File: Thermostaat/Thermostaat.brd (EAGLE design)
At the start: 79.7 x 60.2 mm, 30 parts, among them IC2 MEGA8-P

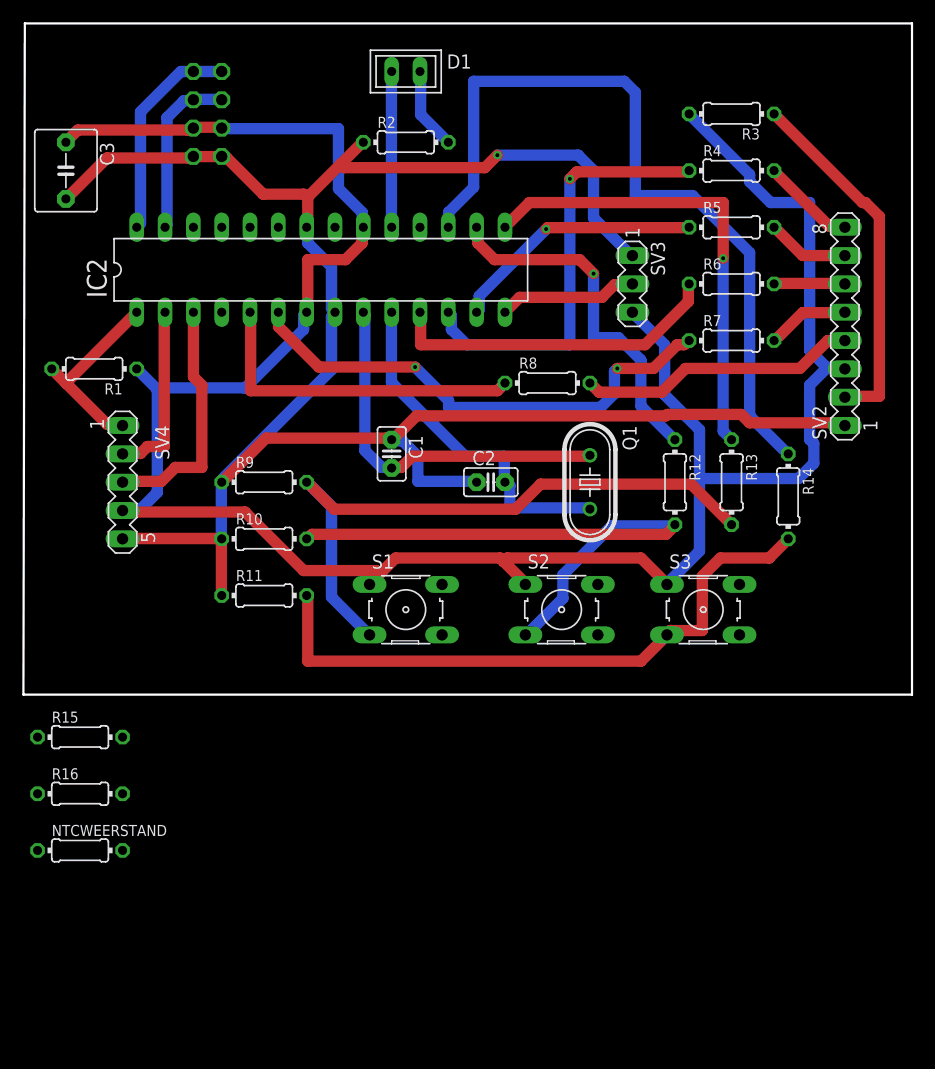
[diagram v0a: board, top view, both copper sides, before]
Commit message: transistor toegevoegd voor relais
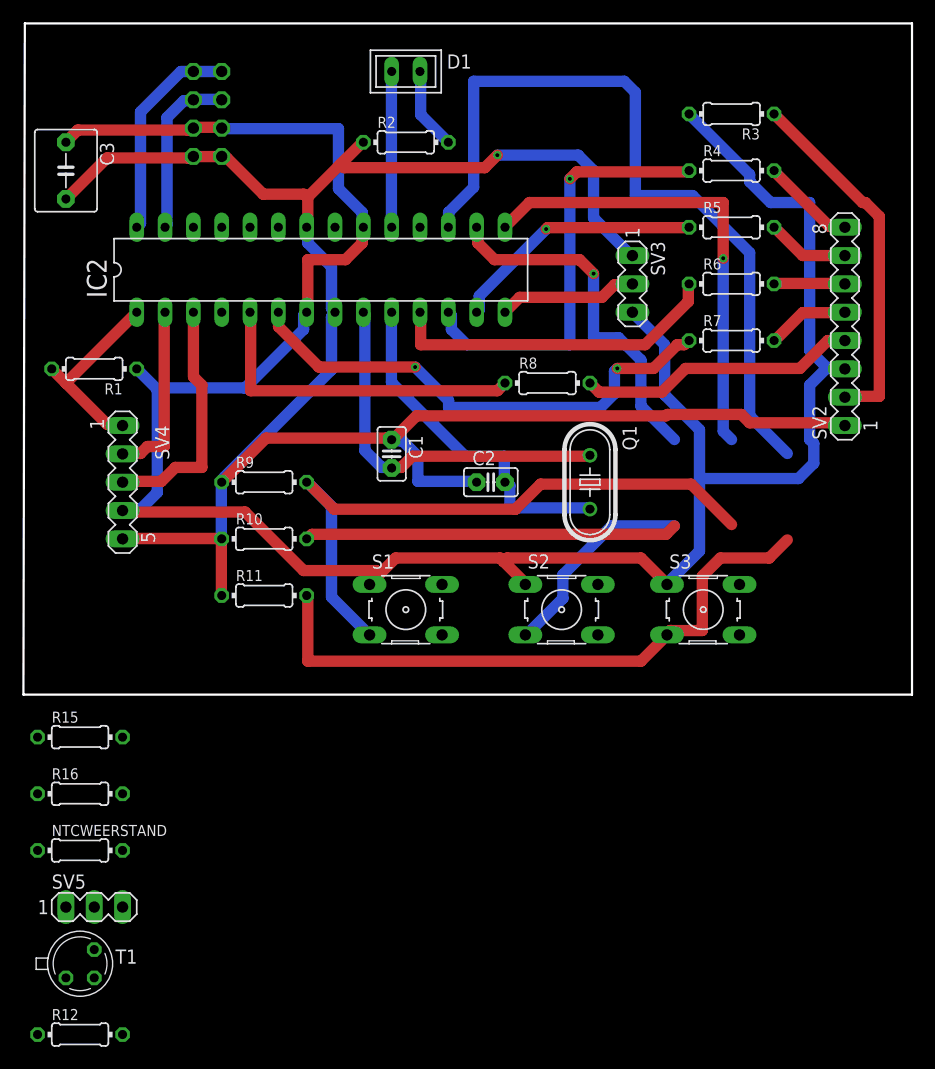
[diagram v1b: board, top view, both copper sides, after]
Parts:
- removed R13, R14: 10k, rcl:0204/7
- added SV5: (no value), con-lstb:MA03-1
- added T1: 2N2222, transistor:TO18
- moved R12 72.8 mm to (5.08, -30.5), turned to 0 degrees
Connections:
- removed net N$21: IC2.17, R14.1
- new net N$5: IC2.24, SV5.2
- net GND: now also SV5.1
- net N$18: now also SV3.2, T1.1; no longer IC2.16, R12.1
- net N$19: now also R12.2, T1.2; no longer IC2.15, R13.1
- net N$20: now also R12.1; no longer SV3.2
- net N$25: now also IC2.17; no longer R14.2
- net N$26: now also IC2.16; no longer R12.2
- net N$27: now also IC2.15; no longer R13.2
- net VCC: now also SV5.3, T1.3
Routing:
- net N$21: track 70.0 -> 0.00 mm
- net N$25: track 56.5 -> 126.3 mm
- net N$19: track 42.1 -> 0.00 mm, vias 1 -> 0
- net N$27: track 57.6 -> 99.6 mm, vias 0 -> 1
- net N$18: track 32.2 -> 0.00 mm, vias 1 -> 0
- net N$26: track 52.3 -> 84.3 mm, vias 0 -> 1
